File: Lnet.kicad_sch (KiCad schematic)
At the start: 10 parts, among them J6 RJ12, J7 RJ12, Q2 AO3400A, U5 LM311

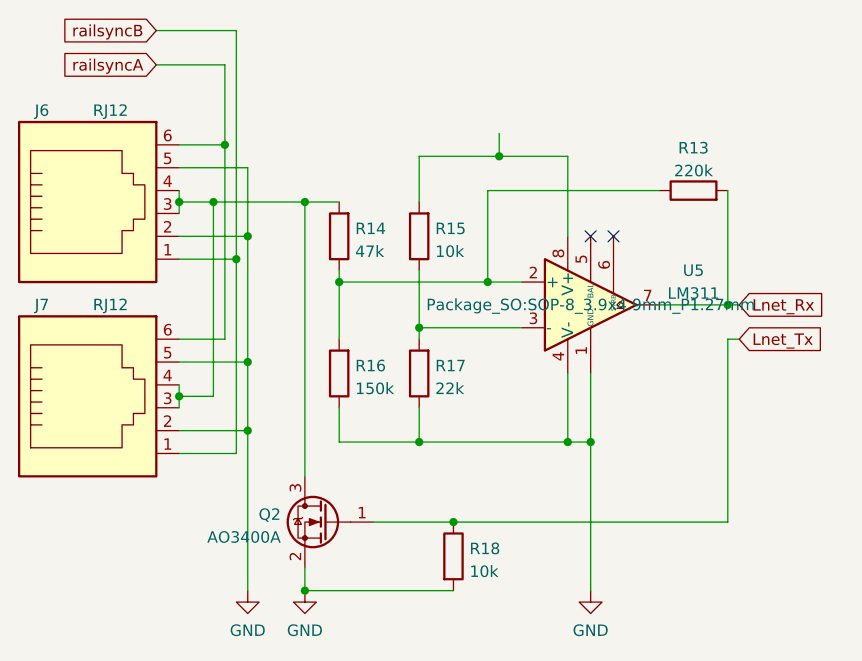
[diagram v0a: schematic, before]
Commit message: added 2 missing cheamtic sheets and deleted obsolete sheets
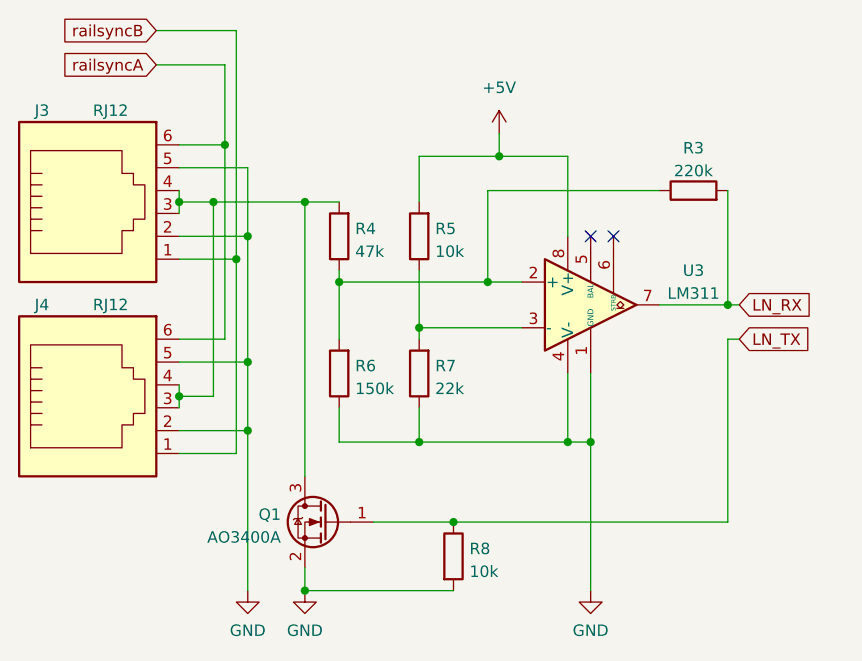
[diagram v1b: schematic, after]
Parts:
- renumbered J6 to J3, J7 to J4, Q2 to Q1, R13 to R3, R14 to R4, R15 to R5, R16 to R6, R17 to R7, R18 to R8, U5 to U3
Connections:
- net +5V: now reaches R5.2, U3.8 (V+)
- net Lnet_Rx renamed LN_RX
- net Lnet_Tx renamed LN_TX
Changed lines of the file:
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@@
     )
   )
-  (global_label "Lnet_Tx" (shape input) (at 142.24 96.52 0) (fields_autoplaced)
+  (global_label "LN_RX" (shape input) (at 142.24 92.71 0) (fields_autoplaced)
     (effects (font (size 1.27 1.27)) (justify left))
-    (property "Intersheet References" "${INTERSHEET_REFS}" (id 0) (at 151.6079 96.4406 0)
-      (effects (font (size 1.27 1.27)) (justify left) hide)
-    )
-  )
-  (global_label "Lnet_Rx" (shape input) (at 142.24 92.71 0) (fields_autoplaced)
-    (effects (font (size 1.27 1.27)) (justify left))
-    (property "Intersheet References" "${INTERSHEET_REFS}" (id 0) (at 151.9102 92.6306 0)
+    (property "Intersheet References" "${INTERSHEET_REFS}" (id 0) (at 150.4588 92.7894 0)
       (effects (font (size 1.27 1.27)) (justify left) hide)
     )
@@
     )
   )
+  (global_label "LN_TX" (shape input) (at 142.24 96.52 0) (fields_autoplaced)
+    (effects (font (size 1.27 1.27)) (justify left))
+    (property "Intersheet References" "${INTERSHEET_REFS}" (id 0) (at 150.1564 96.5994 0)
+      (effects (font (size 1.27 1.27)) (justify left) hide)
+    )
+  )
   (symbol (lib_id "power:GND") (at 93.98 124.46 0) (unit 1)
     (in_bom yes) (on_board yes) (fields_autoplaced)
-    (property "Reference" "#PWR023" (id 0) (at 93.98 130.81 0)
+    (property "Reference" "#PWR020" (id 0) (at 93.98 130.81 0)
       (effects (font (size 1.27 1.27)) hide)
     )
@@
   (symbol (lib_id "power:GND") (at 87.63 124.46 0) (unit 1)
     (in_bom yes) (on_board yes) (fields_autoplaced)
-    (property "Reference" "#PWR022" (id 0) (at 87.63 130.81 0)
+    (property "Reference" "#PWR019" (id 0) (at 87.63 130.81 0)
       (effects (font (size 1.27 1.27)) hide)
     )
@@
   (symbol (lib_id "Comparator:LM311") (at 125.73 92.71 0) (unit 1)
     (in_bom yes) (on_board yes)
-    (property "Reference" "U5" (id 0) (at 137.16 88.9 0))
+    (property "Reference" "U3" (id 0) (at 137.16 88.9 0))
     (property "Value" "LM311" (id 1) (at 137.16 91.44 0))
-    (property "Footprint" "Package_SO:SOP-8_3.9x4.9mm_P1.27mm" (id 2) (at 125.73 92.71 0))
+    (property "Footprint" "Package_SO:SOP-8_3.9x4.9mm_P1.27mm" (id 2) (at 125.73 92.71 0)
+      (effects (font (size 1.27 1.27)) hide)
+    )
     (property "Datasheet" "https://www.st.com/resource/en/datasheet/lm311.pdf" (id 3) (at 125.73 92.71 0)
       (effects (font (size 1.27 1.27)) hide)
@@
   (symbol (lib_id "Device:R") (at 97.79 100.33 180) (unit 1)
     (in_bom yes) (on_board yes) (fields_autoplaced)
-    (property "Reference" "R16" (id 0) (at 99.568 99.4953 0)
+    (property "Reference" "R6" (id 0) (at 99.568 99.4953 0)
       (effects (font (size 1.27 1.27)) (justify right))
     )
@@
   (symbol (lib_id "Device:R") (at 106.68 100.33 180) (unit 1)
     (in_bom yes) (on_board yes) (fields_autoplaced)
-    (property "Reference" "R17" (id 0) (at 108.458 99.4953 0)
+    (property "Reference" "R7" (id 0) (at 108.458 99.4953 0)
       (effects (font (size 1.27 1.27)) (justify right))
     )
@@
   (symbol (lib_id "Device:R") (at 97.79 85.09 180) (unit 1)
     (in_bom yes) (on_board yes) (fields_autoplaced)
-    (property "Reference" "R14" (id 0) (at 99.568 84.2553 0)
+    (property "Reference" "R4" (id 0) (at 99.568 84.2553 0)
       (effects (font (size 1.27 1.27)) (justify right))
     )
@@
   (symbol (lib_id "Device:R") (at 110.49 120.65 0) (unit 1)
     (in_bom yes) (on_board yes) (fields_autoplaced)
-    (property "Reference" "R18" (id 0) (at 112.268 119.8153 0)
+    (property "Reference" "R8" (id 0) (at 112.268 119.8153 0)
       (effects (font (size 1.27 1.27)) (justify left))
     )
@@
   (symbol (lib_id "Transistor_FET:AO3400A") (at 96.52 116.84 0) (mirror y) (unit 1)
     (in_bom yes) (on_board yes) (fields_autoplaced)
-    (property "Reference" "Q2" (id 0) (at 91.3131 116.0053 0)
+    (property "Reference" "Q1" (id 0) (at 91.3131 116.0053 0)
       (effects (font (size 1.27 1.27)) (justify left))
     )
@@
   (symbol (lib_id "Connector:RJ12") (at 69.85 82.55 0) (unit 1)
     (in_bom yes) (on_board yes)
-    (property "Reference" "J6" (id 0) (at 64.77 71.12 0))
+    (property "Reference" "J3" (id 0) (at 64.77 71.12 0))
     (property "Value" "RJ12" (id 1) (at 72.39 71.12 0))
     (property "Footprint" "Connector_RJ:RJ25_Wayconn_MJEA-660X1_Horizontal" (id 2) (at 69.85 81.915 90)
@@
   (symbol (lib_id "Connector:RJ12") (at 69.85 104.14 0) (unit 1)
     (in_bom yes) (on_board yes)
-    (property "Reference" "J7" (id 0) (at 64.77 92.71 0))
+    (property "Reference" "J4" (id 0) (at 64.77 92.71 0))
     (property "Value" "RJ12" (id 1) (at 72.39 92.71 0))
     (property "Footprint" "Connector_RJ:RJ25_Wayconn_MJEA-660X1_Horizontal" (id 2) (at 69.85 103.505 90)
@@
   (symbol (lib_id "Device:R") (at 106.68 85.09 180) (unit 1)
     (in_bom yes) (on_board yes) (fields_autoplaced)
-    (property "Reference" "R15" (id 0) (at 108.458 84.2553 0)
+    (property "Reference" "R5" (id 0) (at 108.458 84.2553 0)
       (effects (font (size 1.27 1.27)) (justify right))
     )
@@
     (pin "2")
   )
+  (symbol (lib_id "power:+5V") (at 115.57 73.66 0) (unit 1)
+    (in_bom yes) (on_board yes) (fields_autoplaced)
+    (property "Reference" "#PWR018" (id 0) (at 115.57 77.47 0)
+      (effects (font (size 1.27 1.27)) hide)
+    )
+    (property "Value" "+5V" (id 1) (at 115.57 68.58 0))
+    (property "Footprint" "" (id 2) (at 115.57 73.66 0)
+      (effects (font (size 1.27 1.27)) hide)
+    )
+    (property "Datasheet" "" (id 3) (at 115.57 73.66 0)
+      (effects (font (size 1.27 1.27)) hide)
+    )
+    (pin "1")
+  )
   (symbol (lib_id "power:GND") (at 125.73 124.46 0) (unit 1)
     (in_bom yes) (on_board yes) (fields_autoplaced)
-    (property "Reference" "#PWR024" (id 0) (at 125.73 130.81 0)
+    (property "Reference" "#PWR021" (id 0) (at 125.73 130.81 0)
       (effects (font (size 1.27 1.27)) hide)
     )
@@
   (symbol (lib_id "Device:R") (at 137.16 80.01 90) (unit 1)
     (in_bom yes) (on_board yes) (fields_autoplaced)
-    (property "Reference" "R13" (id 0) (at 137.16 75.2942 90))
+    (property "Reference" "R3" (id 0) (at 137.16 75.2942 90))
     (property "Value" "220k" (id 1) (at 137.16 77.8311 90))
     (property "Footprint" "Resistor_SMD:R_0805_2012Metric_Pad1.20x1.40mm_HandSolder" (id 2) (at 137.16 81.788 90)
